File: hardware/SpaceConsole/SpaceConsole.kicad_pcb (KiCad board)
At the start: 2 copper layers, 80 x 55.9 mm, 19 parts, among them IC1 ArduinoProMini, J1 LeftFrontLED, J2 RightFrontLED, J3 LeftMiddleLED, J4 RightMiddleLED, J5 RearLED, J6 SwitchA, J7 Battery, J8 Conn_01x09_Male, J9 Power_Switch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

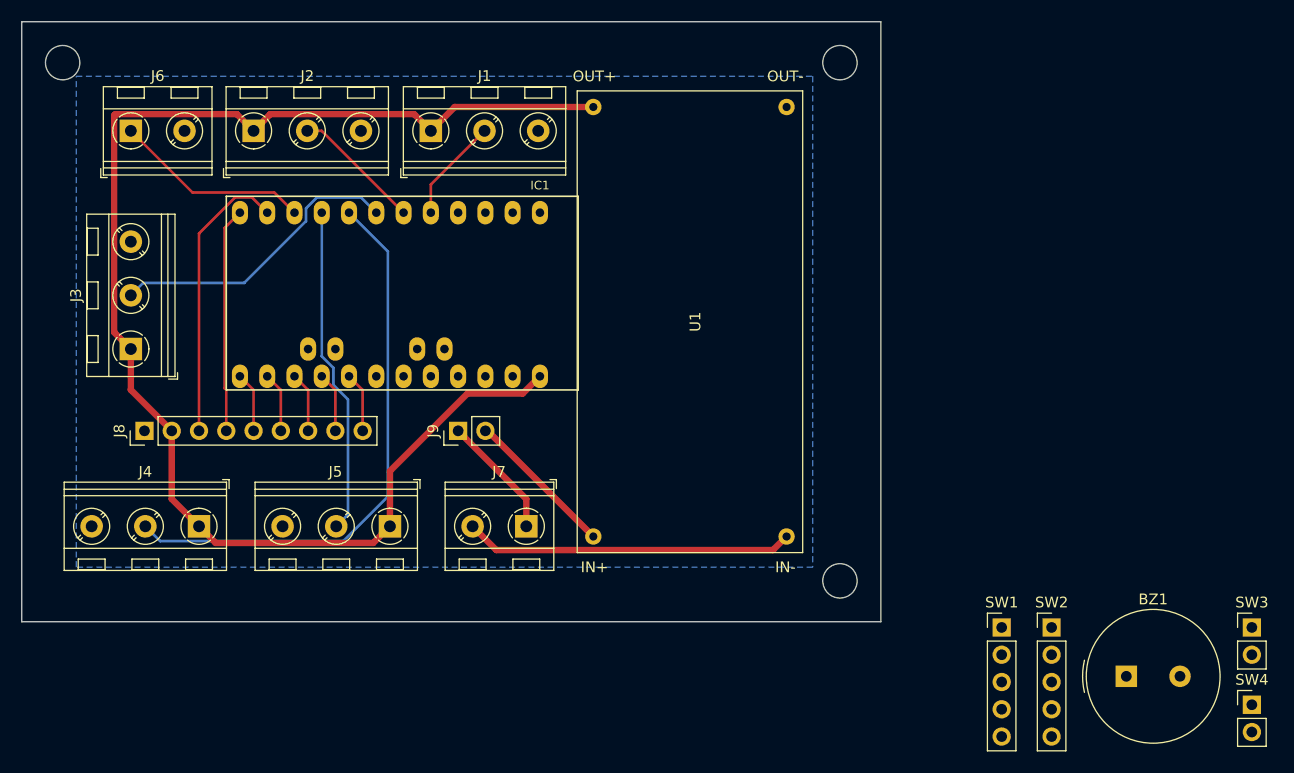
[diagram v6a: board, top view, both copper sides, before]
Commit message: Add routing for knobs and switches
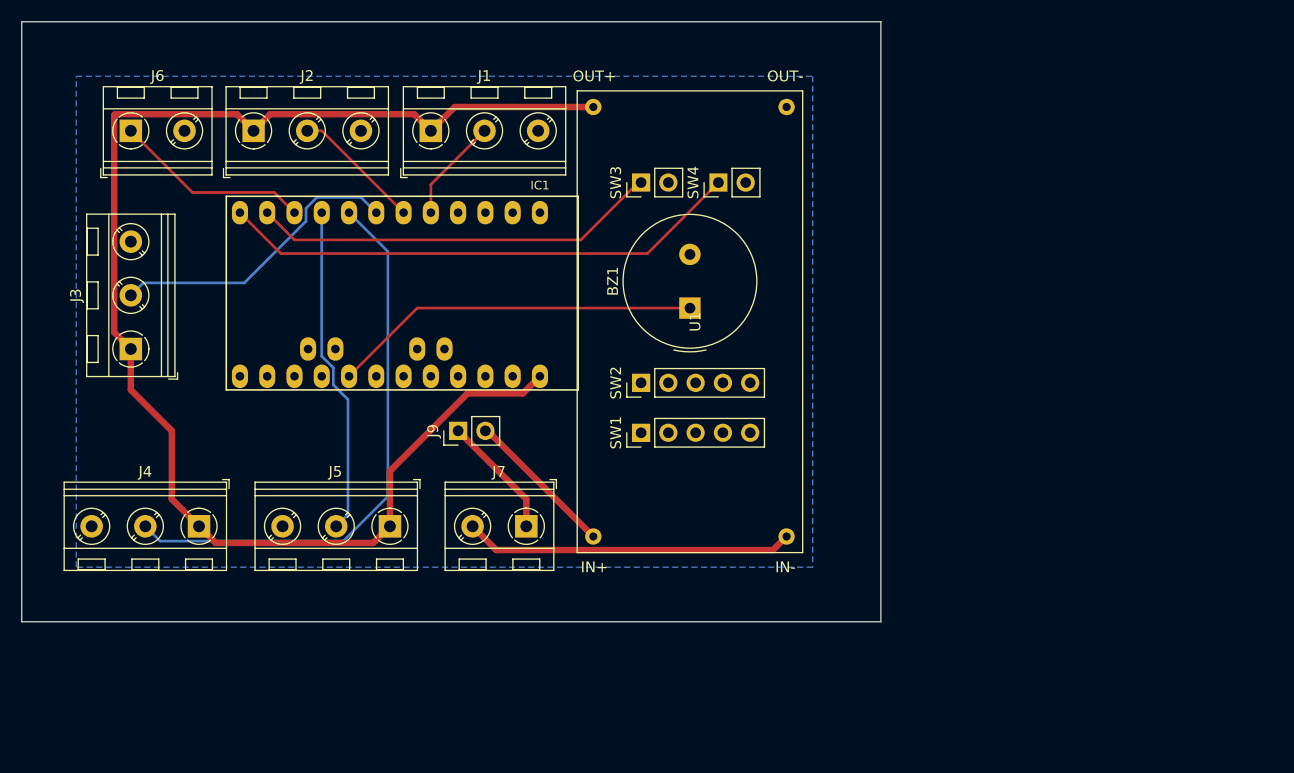
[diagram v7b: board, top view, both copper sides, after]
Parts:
- removed J8: Conn_01x09_Male, Connector_PinHeader_2.54mm:PinHeader_1x09_P2.54mm_Vertical
- removed REF** (x3): MountingHole_3.2mm_M3, MountingHole:MountingHole_3.2mm_M3
- moved SW3 70.4 mm to (187.2, 88.6), turned to 90 degrees
- moved SW4 69.5 mm to (194.4, 88.6), turned to 90 degrees
- moved BZ1 53.2 mm to (191.8, 100.3), turned to 90 degrees
- moved SW2 44.5 mm to (187.2, 107.3), turned to 90 degrees
- moved SW1 38.2 mm to (187.2, 111.9), turned to 90 degrees
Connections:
- net Net-(J7-Pad1) renamed /Battery+
- U1 pad 1: Net-(U1-Pad1) -> Net-(J9-Pad2)
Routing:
- net /HornOut: track 5.61 -> 34.4 mm
- net /SwitchC: track 21.0 -> 48.9 mm
- net /SwitchB: track 26.7 -> 38.1 mm
- net /KnobB1: track 5.61 -> 0.00 mm
- net /KnobB0: track 5.61 -> 0.00 mm
- net /KnobA1: track 5.61 -> 0.00 mm
- net /KnobA0: track 5.61 -> 0.00 mm

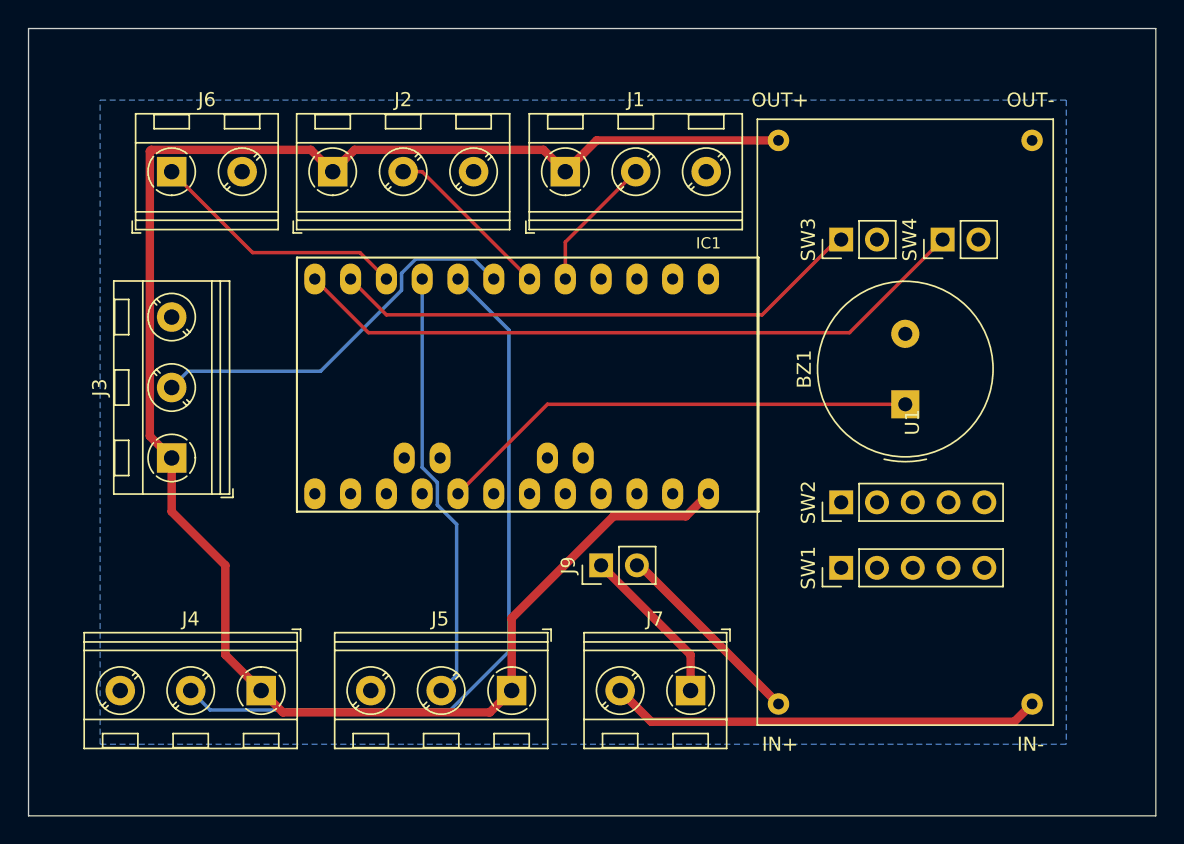
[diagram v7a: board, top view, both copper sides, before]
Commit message: Move knobs and switches to back, readd drill holes
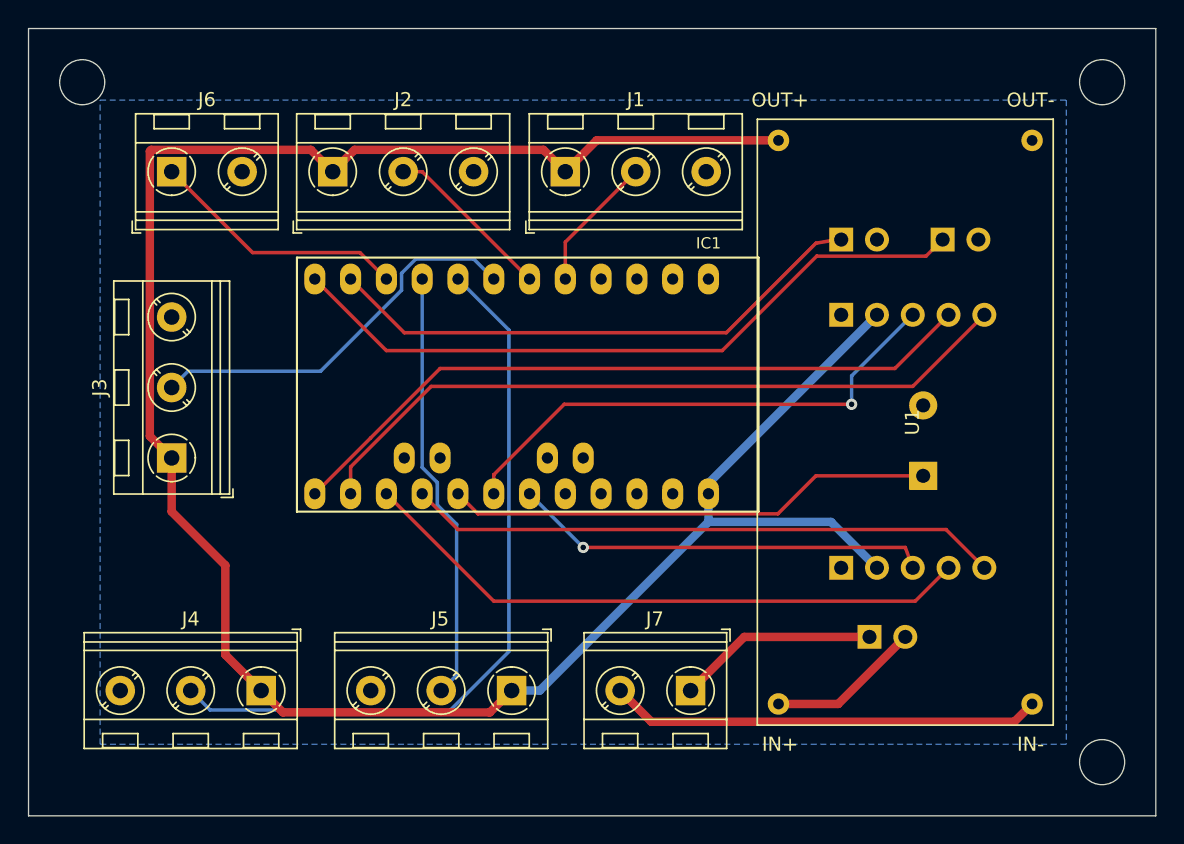
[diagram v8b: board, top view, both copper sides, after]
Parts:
- added REF**: MountingHole_3.2mm_M3, MountingHole:MountingHole_3.2mm_M3, F.Cu at (205.7, 125.7)
- added REF**: MountingHole_3.2mm_M3, MountingHole:MountingHole_3.2mm_M3, F.Cu at (205.7, 77.5)
- added REF**: MountingHole_3.2mm_M3, MountingHole:MountingHole_3.2mm_M3, F.Cu at (133.3, 77.5)
- BZ1, J9, SW1, SW2, SW3, SW4: moved to B.Cu
- moved J9 19.7 mm to (189.2, 116.8), turned to 270 degrees
- moved SW2 13.3 mm to (187.2, 94.0), turned to 270 degrees
- moved BZ1 5.24 mm to (193.0, 105.4)
- turned SW1 to 270 degrees
- turned SW3 to 270 degrees
- turned SW4 to 270 degrees
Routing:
- net /KnobA1: track 0.00 -> 51.4 mm
- net /KnobA0: track 0.00 -> 50.2 mm
- net /KnobB0: track 0.00 -> 44.0 mm
- net /KnobB1: track 0.00 -> 42.1 mm
- net /SwitchD: track 0.00 -> 37.0 mm, vias 0 -> 1
- net /SwitchE: track 0.00 -> 29.8 mm, vias 0 -> 1
- net VCC: track 130.9 -> 160.0 mm
- net Net-(J9-Pad2): track 14.1 -> 11.0 mm
- net /Battery+: track 11.5 -> 14.3 mm
- net /SwitchC: track 48.9 -> 49.9 mm
- net /SwitchB: track 38.1 -> 39.1 mm
